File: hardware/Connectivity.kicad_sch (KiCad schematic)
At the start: 12 parts, among them U6 MCP2542FD-E/MF, U7 MCP2542FD-E/MF

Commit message: schematic done
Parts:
- added D11: ESDA5V3SC5, Package_TO_SOT_SMD:SOT-23-6, symbol Power_Protection:ESDA5V3SC5
- added D13: ESDA25SC6Y, Package_TO_SOT_SMD:SOT-23-6, symbol Power_Protection:ESDA5V3SC5
- added Q18, Q19, Q20: 2N7002, Package_TO_SOT_SMD:SOT-23, symbol Transistor_FET:2N7002
- added R4, R5, R6: 10k, Resistor_SMD:R_0603_1608Metric, symbol Device:R_Small
- added RN2: 4x200, Resistor_SMD:R_Array_Convex_4x0603, symbol Device:R_Pack04
- added RN7: 4x1k, Resistor_SMD:R_Array_Convex_4x0603, symbol Device:R_Pack04
- added U5, U8, U9: TLP2310, Package_SO:SO-5_4.4x3.6mm_P1.27mm, symbol Isolator:TLP2310
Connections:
- net GND: now also D11.2 (K), D11.5 (NC), D13.2 (K), D13.5 (NC), U5.3 (K), U5.4 (GND), U8.3 (K), U8.4 (GND), U9.3 (K), U9.4 (GND)
- net MCU_D+: now also D8.4 (A); no longer D8.3 (A)
- net MCU_D-: now also D8.3 (A); no longer D8.4 (A)
- net +3V3 renamed +3.3V
- net +3.3V: now also Q18.1 (G), Q19.1 (G), Q20.1 (G), RN7.2 (R2.1), RN7.3 (R3.1), RN7.4 (R4.1), U5.6 (VDD), U8.6 (VDD), U9.6 (VDD)
- net IN1 renamed SPI_O1
- net IN2 renamed SPI_O2
- net IN3 renamed SPI_O3
- net IN4 renamed SPI_O4
- net OUT1 renamed SPI_I1
- net OUT2 renamed SPI_I2
- net OUT3 renamed SPI_I3
- net OUT4 renamed SPI_I4
- new net: R4.1, U5.1 (A)
- new net: R5.1, U8.1 (A)
- new net: R6.1, U9.1 (A)
- new net AIR1_I: D13.1 (A), Q18.2 (S)
- new net AIR1_O: Q18.3 (D), RN7.5 (R4.2)
- new net AIR2_I: D13.3 (A), Q19.2 (S)
- new net AIR2_O: Q19.3 (D), RN7.6 (R3.2)
- new net AIR3_I: D13.4 (A), Q20.2 (S)
- new net AIR3_O: Q20.3 (D), RN7.7 (R2.2)
- new net BOOT0_I: RN2.3 (R3.1)
- new net BOOT0_O: D11.3 (A), RN2.6 (R3.2)
- new net MV_I1: R4.2
- new net MV_I2: R5.2
- new net MV_I3: R6.2
- new net MV_O1: U5.5 (VO)
- new net MV_O2: U8.5 (VO)
- new net MV_O3: U9.5 (VO)
- new net NRST_I: RN2.2 (R2.1)
- new net NRST_O: D11.4 (A), RN2.7 (R2.2)
- no-connect marks 2 -> 11
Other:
- note added: "AIR DETECT"
- note added: "MCU DEBUG"
- note added: "MEDIUM VOLTAGE INPUTS"
- note added: "SPI"
- moved on the sheet: C32, C33, C37, C38, D12, D8, FL1, R7, R8, RN17, U6, U7

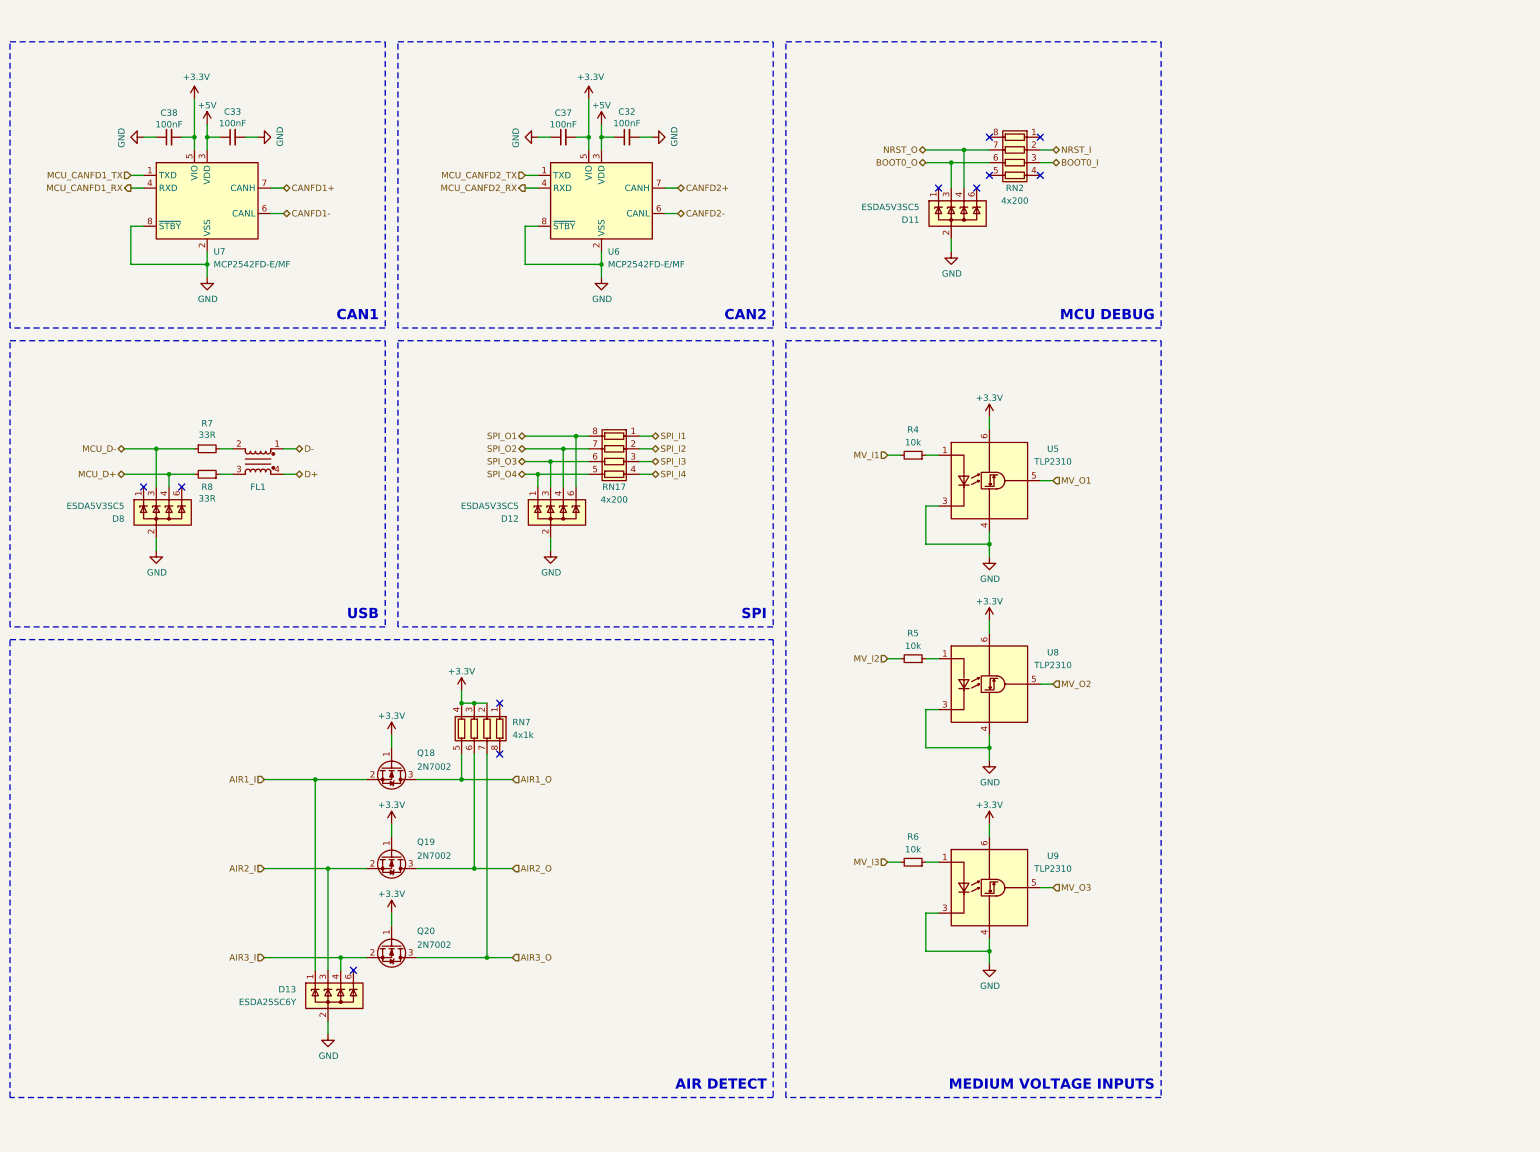
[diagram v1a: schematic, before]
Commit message: new firmware for bga version of stm, change stm from smt to bga, smaller HV dividers, added 3rd can transciver, and other
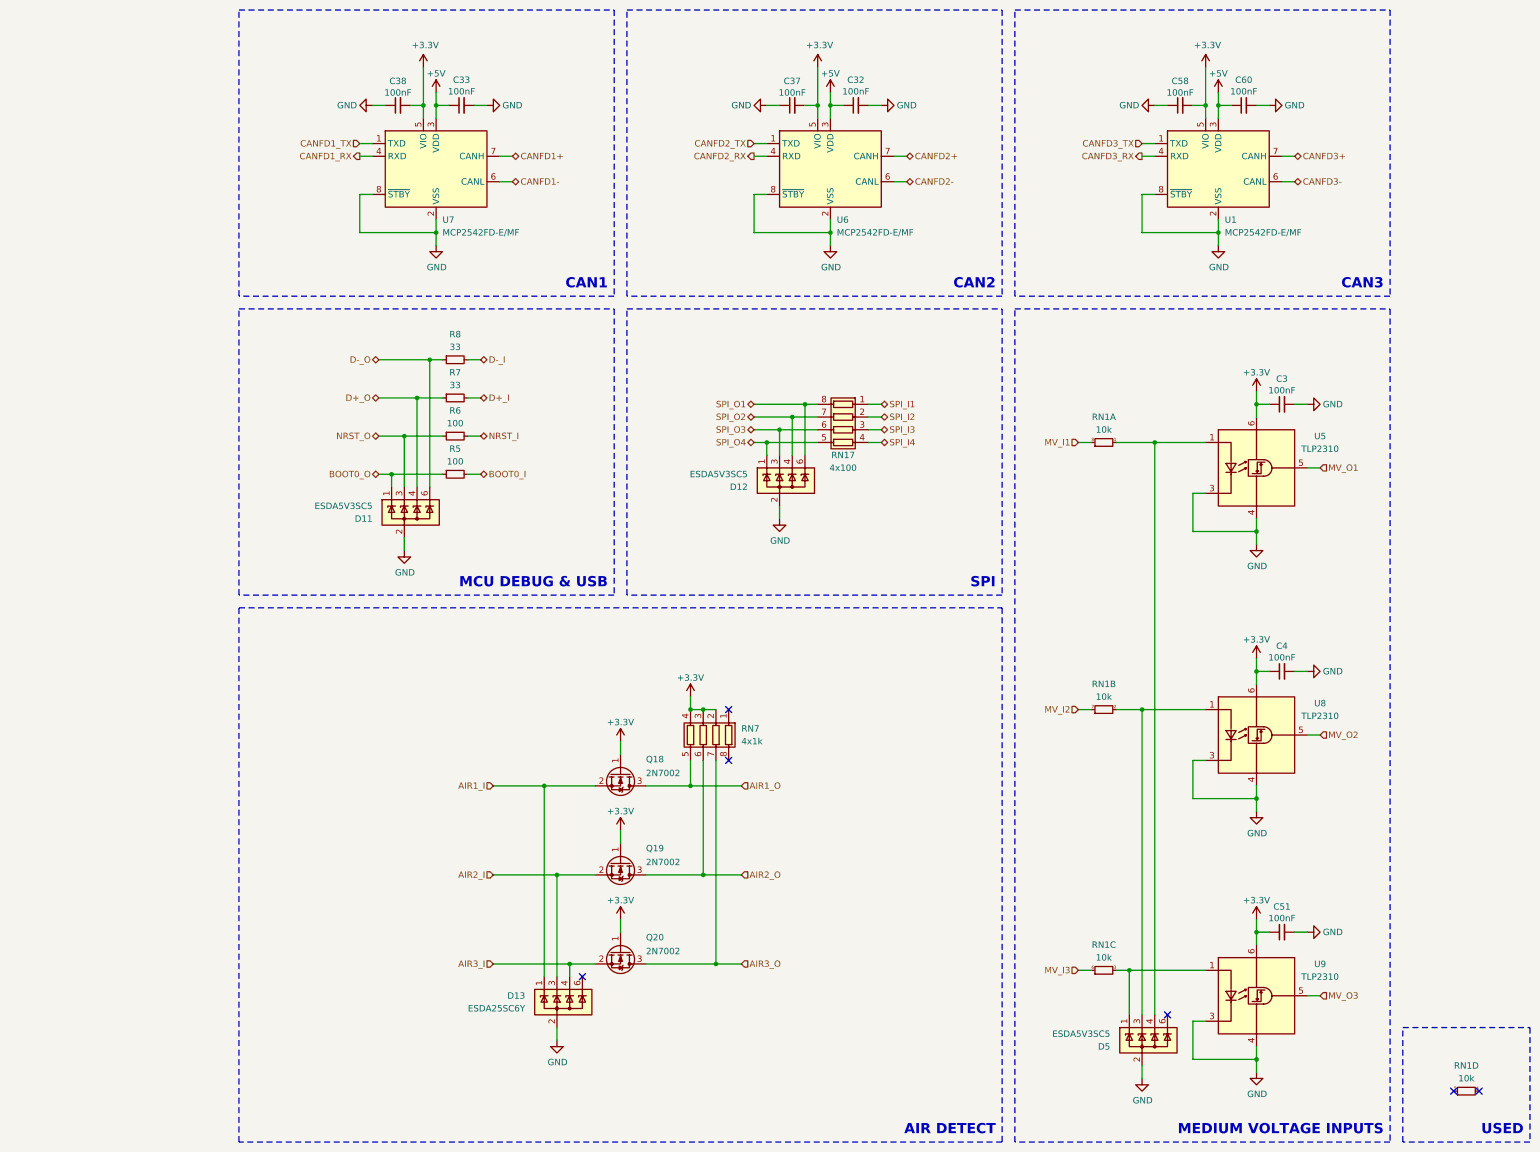
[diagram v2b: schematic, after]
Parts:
- removed D8: ESDA5V3SC5, Package_TO_SOT_SMD:SOT-23-6, symbol Power_Protection:ESDA5V3SC5
- removed FL1: Choke_Coilcraft_0603USB-142, Inductor_SMD:L_CommonModeChoke_Coilcraft_0603USB, symbol Filter:Choke_Coilcraft_0603USB-142
- removed R4: 10k, Resistor_SMD:R_0603_1608Metric, symbol Device:R_Small
- removed RN2: 4x200, Resistor_SMD:R_Array_Convex_4x0603, symbol Device:R_Pack04
- added C3, C4, C51, C58, C60: 100nF, Capacitor_SMD:C_0603_1608Metric, symbol Device:C_Small
- added D5: ESDA5V3SC5, Package_TO_SOT_SMD:SOT-23-6, symbol Power_Protection:ESDA5V3SC5
- added RN1: 10k, Resistor_SMD:R_Array_Convex_4x0603, symbol Device:R_Pack04_Split
- added U1: MCP2542FD-E/MF, Package_DFN_QFN:DFN-8-1EP_3x3mm_P0.65mm_EP1.55x2.4mm, symbol Interface_CAN_LIN:MCP2542FDxMF
- C37, C38: footprint Capacitor_SMD:C_0805_2012Metric -> Capacitor_SMD:C_0603_1608Metric
- R5, R6: value 10k -> 100
- R7, R8: value 33R -> 33
- RN17: value 4x200 -> 4x100
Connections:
- net +3.3V: now also C3.1, C4.1, C51.1, C58.2, U1.5 (VIO)
- net +5V: now also C60.1, U1.3 (VDD)
- net BOOT0_I: now also R5.2
- net BOOT0_O: now also D11.1 (A), R5.1; no longer D11.3 (A)
- net GND: now also C3.2, C4.2, C51.2, C58.1, C60.2, D5.2 (K), D5.5 (NC), U1.2 (VSS), U1.8 (~{STBY}), U1.9 (VSS)
- net MV_I1: now also RN1.8 (R1.2)
- net MV_I2: now also RN1.7 (R2.2); no longer R5.2
- net MV_I3: now also RN1.6 (R3.2); no longer R6.2
- net NRST_I: now also R6.2
- net NRST_O: now also D11.3 (A), R6.1; no longer D11.4 (A)
- net at U5.1 (A): now also D5.4 (A), RN1.1 (R1.1)
- net D-_O: now reaches D11.6 (A)
- net D-_O: now also R8.1
- net at U8.1 (A): now also D5.3 (A), RN1.2 (R2.1); no longer R5.1
- net at U9.1 (A): now also D5.1 (A), RN1.3 (R3.1); no longer R6.1
- net D+_I: now reaches R7.2
- net MCU_CANFD1_RX renamed CANFD1_RX
- net MCU_CANFD1_TX renamed CANFD1_TX
- net MCU_CANFD2_RX renamed CANFD2_RX
- net MCU_CANFD2_TX renamed CANFD2_TX
- net MCU_D+ renamed D-_I
- net MCU_D- renamed D+_O
- net D+_O: now also D11.4 (A)
- new net CANFD3+: U1.7 (CANH)
- new net CANFD3-: U1.6 (CANL)
- new net CANFD3_RX: U1.4 (RXD)
- new net CANFD3_TX: U1.1 (TXD)
- no-connect marks 11 -> 6
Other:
- note added: "CAN3"
- note added: "MCU DEBUG & USB"
- note added: "USED"
- note removed: "MCU DEBUG"
- note removed: "USB"
- moved on the sheet: C32, C33, C37, C38, D11, D12, D13, Q18, Q19, Q20, RN17, RN7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

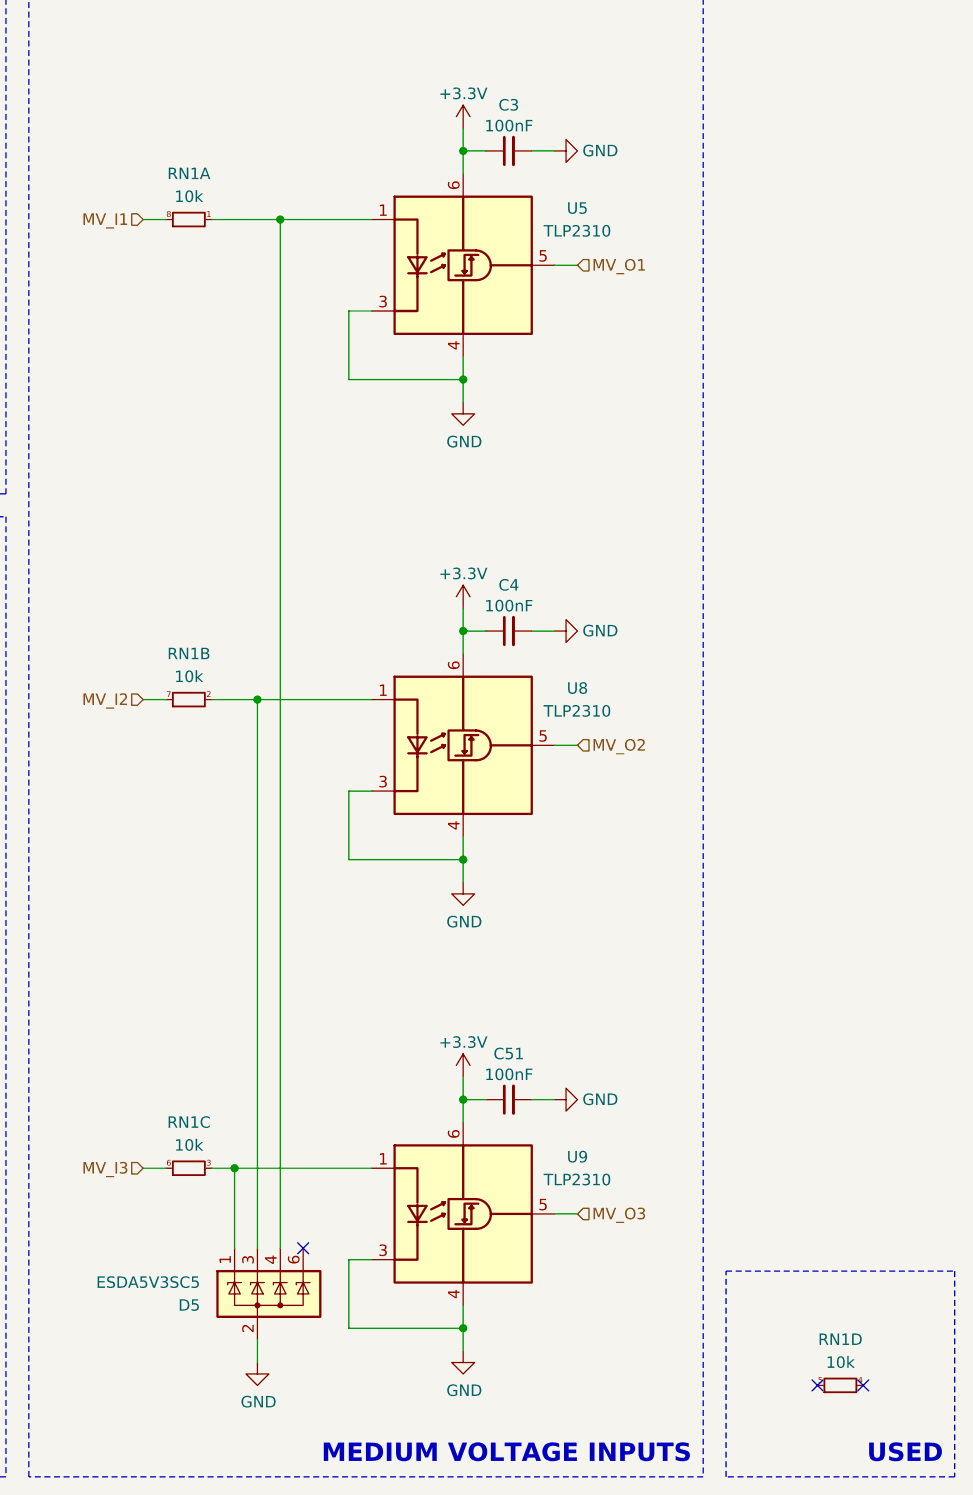
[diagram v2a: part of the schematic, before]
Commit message: mcu pinout done
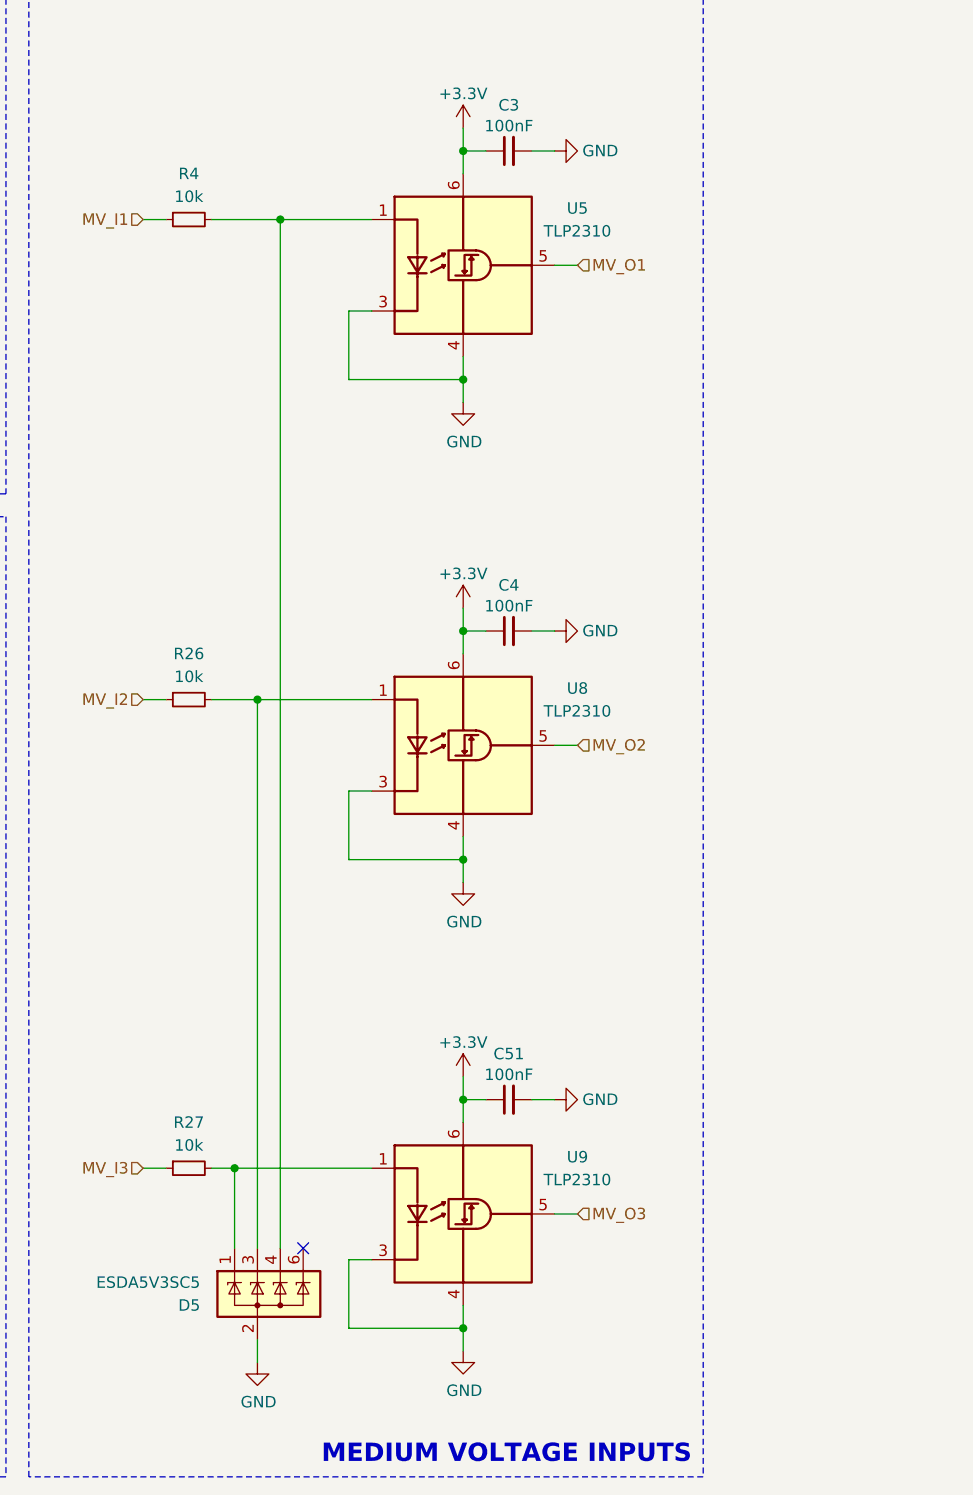
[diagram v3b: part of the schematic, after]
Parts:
- removed RN1: 10k, Resistor_SMD:R_Array_Convex_4x0603, symbol Device:R_Pack04_Split
- added R26, R27, R4: 10k, Resistor_SMD:R_0603_1608Metric, symbol Device:R_Small
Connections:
- net MV_I1: now also R4.1
- net MV_I2: now also R26.1
- net MV_I3: now also R27.1
- net at D5.4 (A), U5.1 (A): now also R4.2
- net at D5.3 (A), U8.1 (A): now also R26.2
- net at D5.1 (A), U9.1 (A): now also R27.2
- no-connect marks 6 -> 4
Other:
- note removed: "USED"

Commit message: mama comit
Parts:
- removed C3, C4, C51: 100nF, Capacitor_SMD:C_0603_1608Metric, symbol Device:C_Small
- removed Q18, Q19, Q20: 2N7002, Package_TO_SOT_SMD:SOT-23, symbol Transistor_FET:2N7002
- removed R5, R6: 100, Resistor_SMD:R_0603_1608Metric, symbol Device:R_Small
- removed U5, U8, U9: TLP2310, Package_SO:SO-5_4.4x3.6mm_P1.27mm, symbol Isolator:TLP2310
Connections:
- net SPI_I1: no longer RN17.1 (R1.1)
- net SPI_I2: no longer RN17.2 (R2.1)
- net SPI_I3: no longer RN17.3 (R3.1)
- net SPI_I4: no longer RN17.4 (R4.1)
- net SPI_O1: no longer D12.6 (A), RN17.8 (R1.2)
- net SPI_O2: no longer D12.4 (A), RN17.7 (R2.2)
- net SPI_O3: no longer D12.3 (A), RN17.6 (R3.2)
- net SPI_O4: no longer D12.1 (A), RN17.5 (R4.2)
- net BOOT0_O: no longer names the net of D11.1 (A)
- net NRST_O: no longer names the net of D11.3 (A)
- new net: D12.1 (A), RN17.5 (R4.2)
- new net: D12.3 (A), RN17.6 (R3.2)
- new net: D12.4 (A), RN17.7 (R2.2)
- new net: D12.6 (A), RN17.8 (R1.2)
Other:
- moved on the sheet: D12, R7, R8, RN17
